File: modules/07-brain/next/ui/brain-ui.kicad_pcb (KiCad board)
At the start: 2 copper layers, 58 x 110 mm, 57 parts, among them J1 Conn_02x03_Odd_Even, J2 Conn_01x02, J3 Conn_01x02, J4 Conn_02x02_Odd_Even, J5 Conn_02x03_Odd_Even, J6 Conn_02x02_Odd_Even, J7 Conn_02x05_Odd_Even, J8 Conn_02x03_Odd_Even, Q1 2N3904, Q2 2N3904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

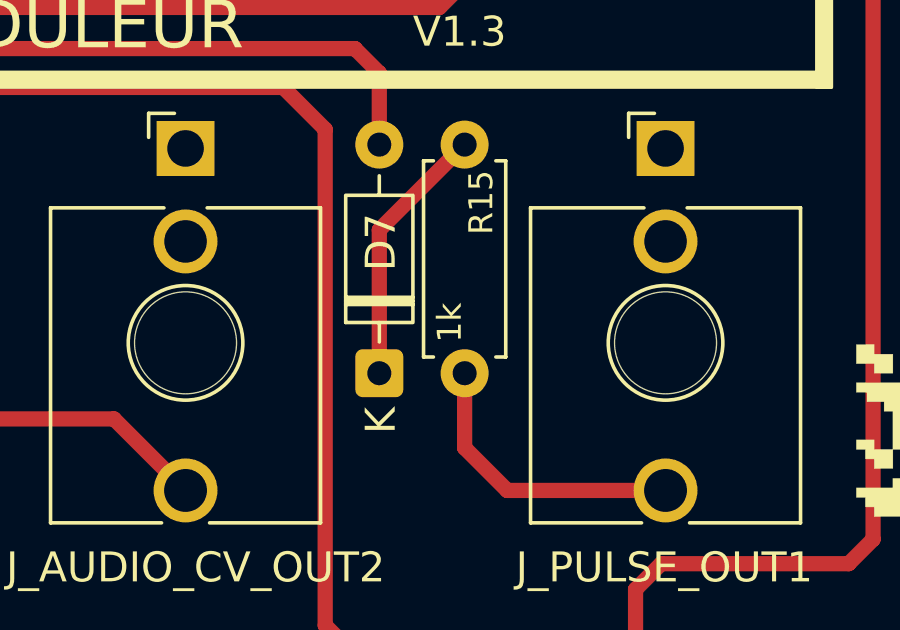
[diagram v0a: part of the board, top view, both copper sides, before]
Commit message: Updated mounting hole H3 on Brain to be grounded
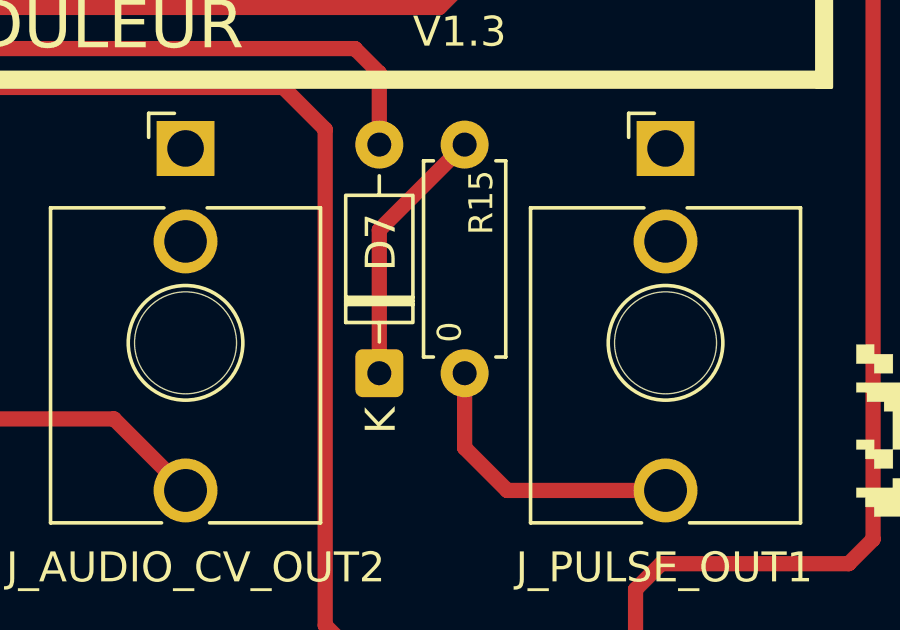
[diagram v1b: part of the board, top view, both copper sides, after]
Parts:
- R15: value 1k -> 0
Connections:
- H3 pad 1: (no net) -> GND
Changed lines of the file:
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@@
 			)
 		)
-		(property "Description" "Mounting Hole without connection"
+		(property "Description" "Mounting Hole with connection"
 			(at 0 0 0)
 			(layer "F.Fab")
@@
 			)
 		)
-		(property ki_fp_filters "MountingHole*")
+		(property "Part No." ""
+			(at 0 0 0)
+			(unlocked yes)
+			(layer "F.Fab")
+			(hide yes)
+			(effects
+				(font
+					(size 1 1)
+					(thickness 0.15)
+				)
+			)
+		)
+		(property ki_fp_filters "MountingHole*Pad*")
 		(sheetname "/")
 		(sheetfile "brain-ui.kicad_sch")
@@
 			(layers "*.Cu" "*.Mask")
 			(remove_unused_layers no)
+			(net 3 "GND")
+			(pinfunction "1")
+			(pintype "input")
 			(zone_connect 2)
 		)
@@
 			)
 		)
-		(property "Value" "1k"
+		(property "Value" "0"
 			(at 6.6 0.5 90)
 			(layer "F.SilkS")
